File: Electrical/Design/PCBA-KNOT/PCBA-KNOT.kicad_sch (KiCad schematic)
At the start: 57 parts, among them CN1 USB-CON-AF-LCP-Offset, J1 MC-107DM, J2 (NF), J3 Conn_01x02, SW1 C2905169, SW2 C2905169, SW3 TC-1109DE-C-G, SW4 ST-0-102-C03-N003-RS, U1 ESP32-S3-WROOM-1U, U2 BL1551B, U3 BL1551B, U4 BL1551B, U5 BL1551B, U6 SESRV05-4, U7 SESRV05-4, U8 74HC165

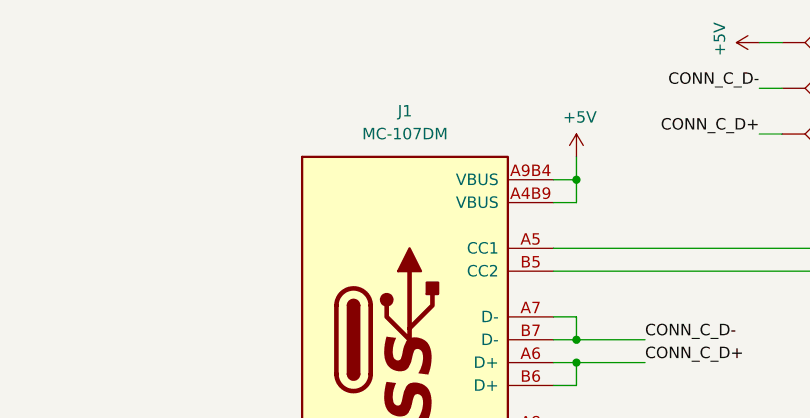
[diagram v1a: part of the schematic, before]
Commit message: SUKU 3d files updated from library
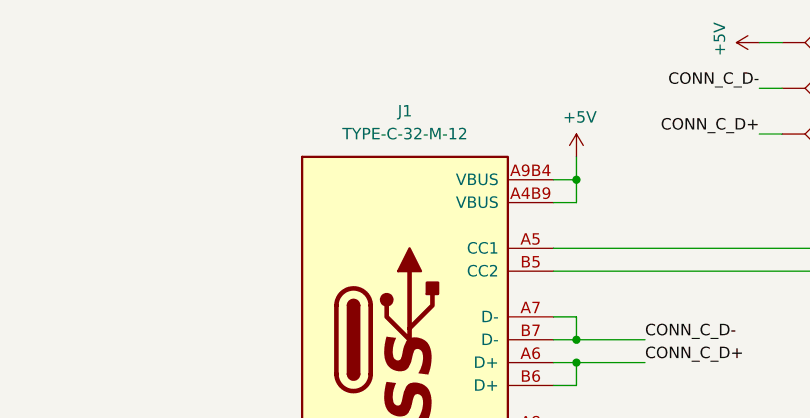
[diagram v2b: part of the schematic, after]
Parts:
- J1: value MC-107DM -> TYPE-C-32-M-12
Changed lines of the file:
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@@
       (effects (font (size 1.27 1.27)))
     )
-    (property "Value" "MC-107DM" (at 171.45 27.94 0)
+    (property "Value" "TYPE-C-32-M-12" (at 171.45 27.94 0)
       (effects (font (size 1.27 1.27)))
     )

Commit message: SUKU 3d files added
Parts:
- CN1: value USB-CON-AF-LCP-Offset -> C42567; footprint suku_basics:USB-A-SMD_AF-LCP-OFFSET -> suku_basics:USB-A-SMD_AF-APPLE-10.6; LCSC Part C42620 -> C42567; Manufacturer ValuePro -> (none)
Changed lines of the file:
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@@
       (effects (font (size 1.27 1.27)) (justify right))
     )
-    (property "Value" "USB-CON-AF-LCP-Offset" (at 276.86 53.3399 0)
+    (property "Value" "C42567" (at 276.86 53.3399 0)
       (effects (font (size 1.27 1.27)) (justify right))
     )
-    (property "Footprint" "suku_basics:USB-A-SMD_AF-LCP-OFFSET" (at 269.24 68.58 0)
+    (property "Footprint" "suku_basics:USB-A-SMD_AF-APPLE-10.6" (at 269.24 68.58 0)
       (effects (font (size 1.27 1.27)) hide)
     )
-    (property "Datasheet" "https://lcsc.com/product-detail/USB-Connectors_A-F-LCPVinyl-pitch17MM-High-temperature_C42620.html" (at 269.24 71.12 0)
+    (property "Datasheet" "" (at 269.24 71.12 0)
       (effects (font (size 1.27 1.27)) hide)
     )
-    (property "Manufacturer" "ValuePro" (at 269.24 73.66 0)
+    (property "Manufacturer" "" (at 269.24 73.66 0)
       (effects (font (size 1.27 1.27)) hide)
     )
-    (property "LCSC Part" "C42620" (at 269.24 76.2 0)
+    (property "LCSC Part" "C42567" (at 269.24 76.2 0)
       (effects (font (size 1.27 1.27)) hide)
     )
